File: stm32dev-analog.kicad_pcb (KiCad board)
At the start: 2 copper layers, 53.3 x 72.4 mm, 55 parts, among them J3 Conn_01x20_Male, J4 Conn_01x20_Male, J8 Conn_02x08_Odd_Even, Q1 LBSS84LT1G, Q2 2N7002, U1 TL072, U2 TL072, U3 TL072, U4 74LVC1T45W6, U5 TL072

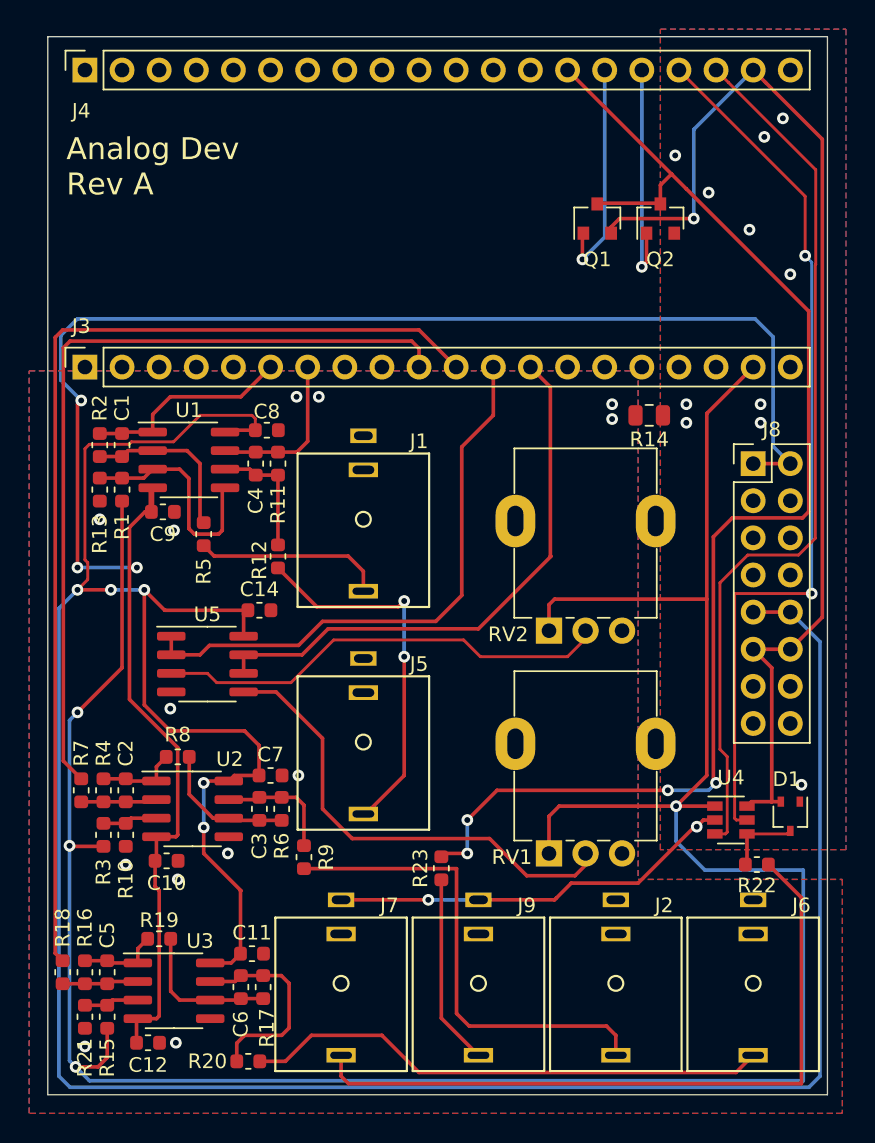
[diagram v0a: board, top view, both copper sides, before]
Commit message: Fixed supply to TL072 of pots.
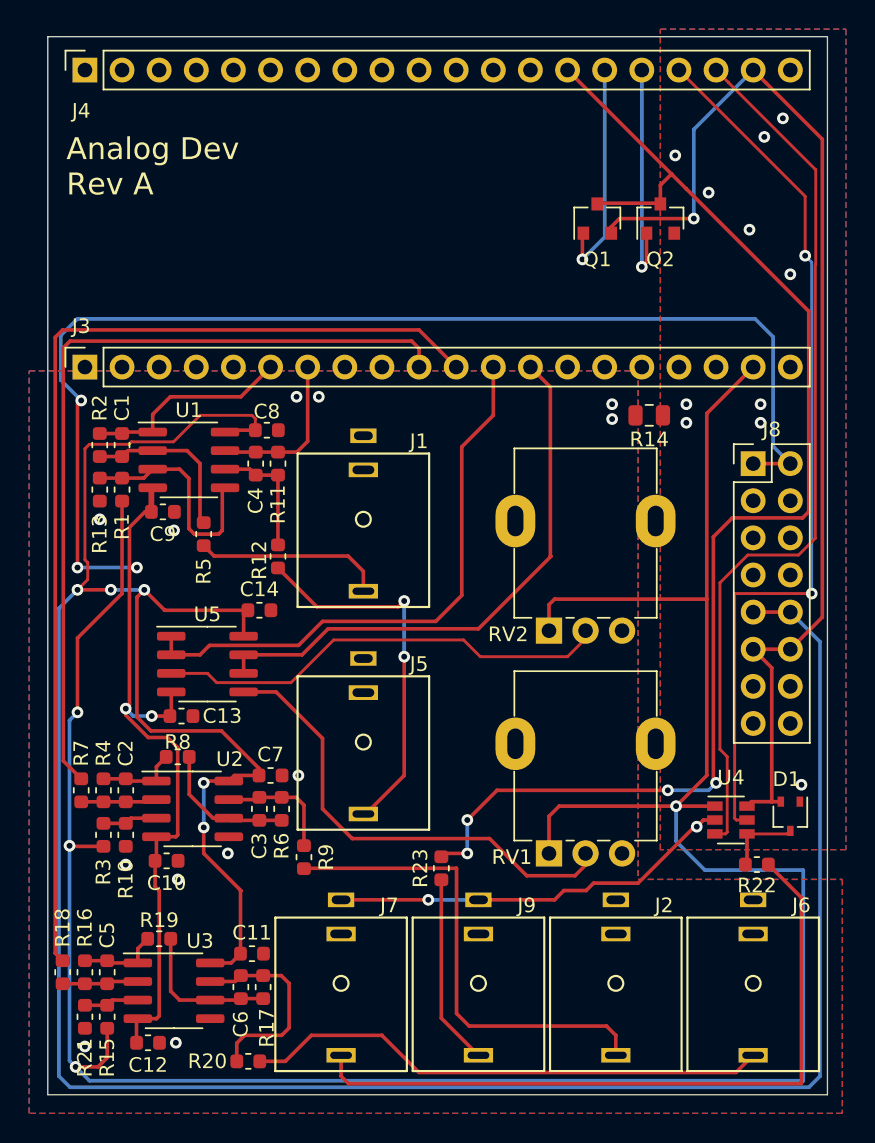
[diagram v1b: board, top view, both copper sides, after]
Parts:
- added C13: 0.1uF, Capacitor_SMD:C_0603_1608Metric, F.Cu at (112.0, 73.2)
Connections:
- U5 pad 4: GNDA -> -12V
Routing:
- net -12V: track 125.7 -> 131.6 mm, vias 3 -> 5
- net GNDA: vias 13 -> 12

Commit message: Changed to 20pF and 200pF resp to use Basic instead of Extended part.
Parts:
- C2: value 18pF -> 20pF
- C5: value 180pF -> 200pF
